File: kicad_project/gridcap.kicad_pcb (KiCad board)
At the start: 2 copper layers, 119.1 x 108.7 mm, 69 parts, among them J1 Conn_01x10

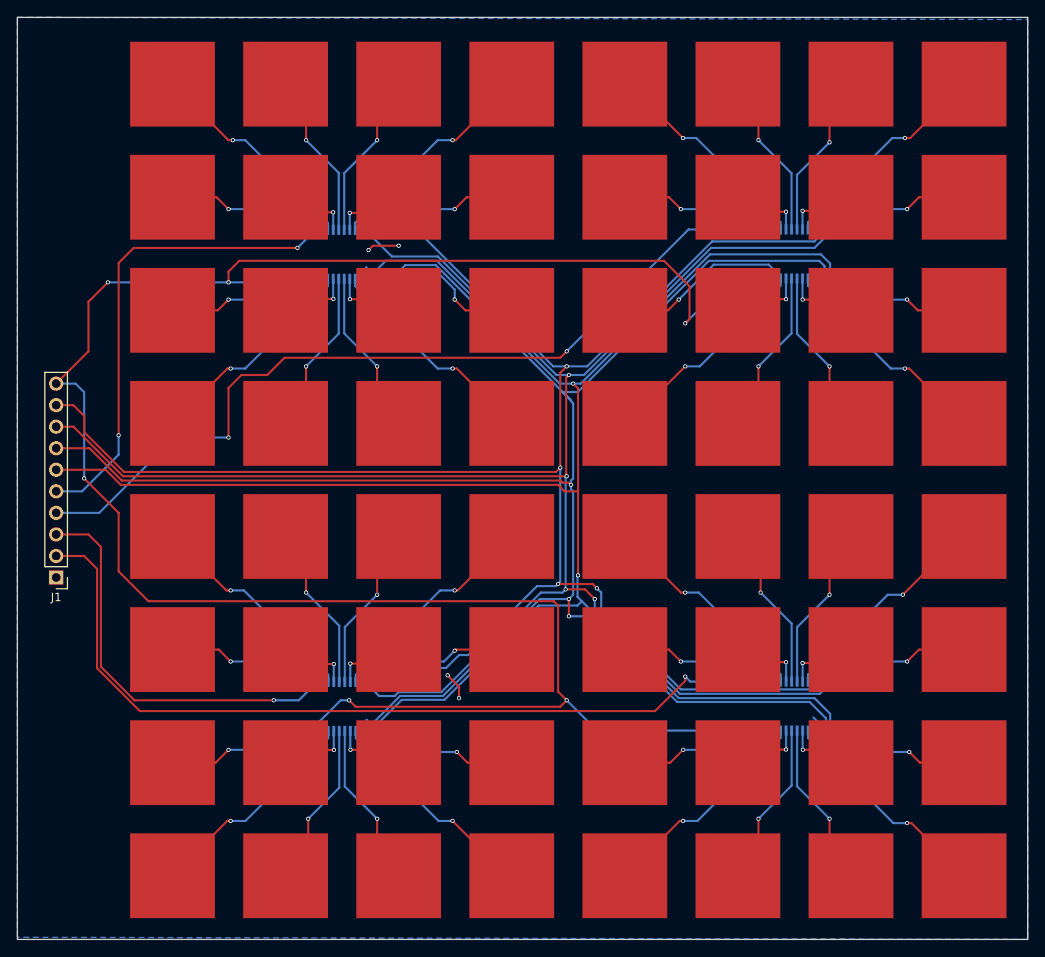
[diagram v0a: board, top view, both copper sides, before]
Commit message: Space out tracks on pcb
Meant to reduce signal noice between tracks
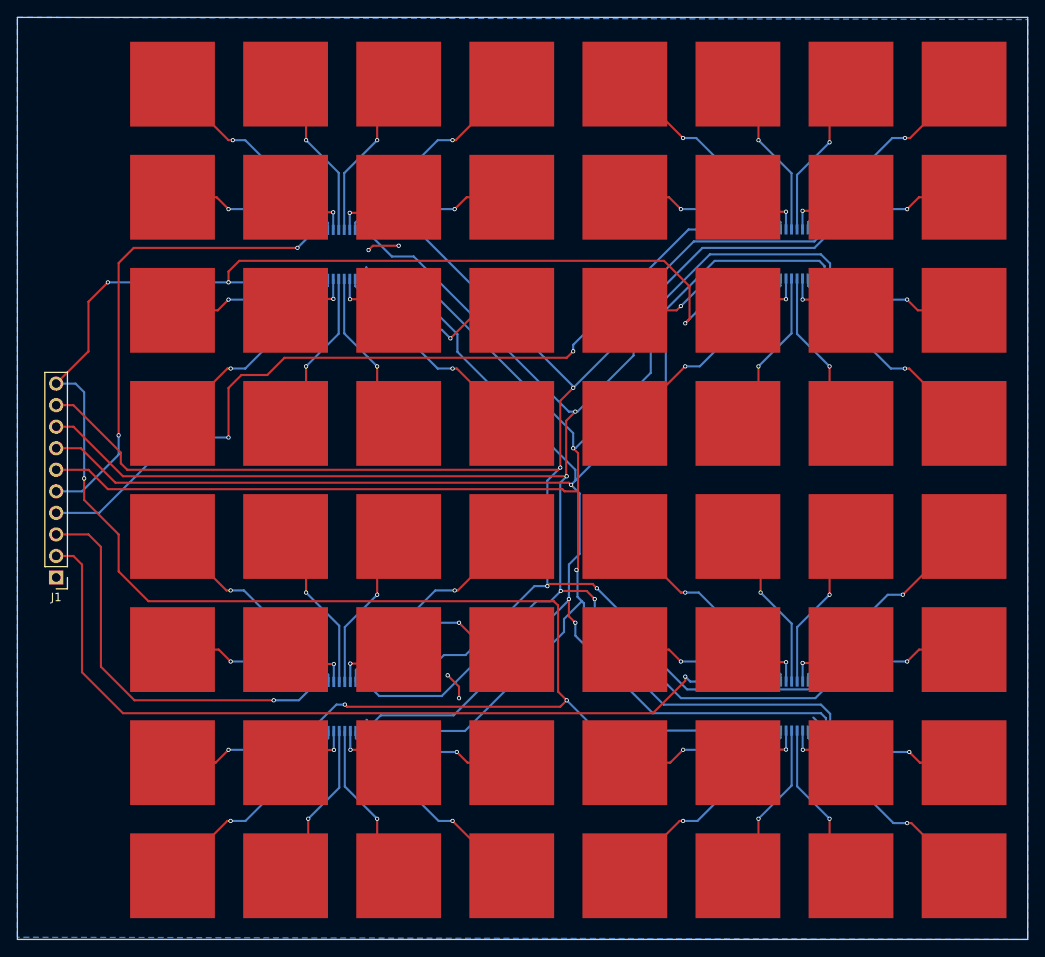
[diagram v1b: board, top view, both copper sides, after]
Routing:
- net S3: track 225.8 -> 229.2 mm
- net S1: track 223.3 -> 226.5 mm
- net S2: track 228.0 -> 231.2 mm
- net Net-(MUX3-Y0): track 19.8 -> 22.4 mm
- net S0: track 224.8 -> 226.3 mm
- net Z4: track 100.8 -> 101.6 mm

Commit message: Make MUX-pads longer
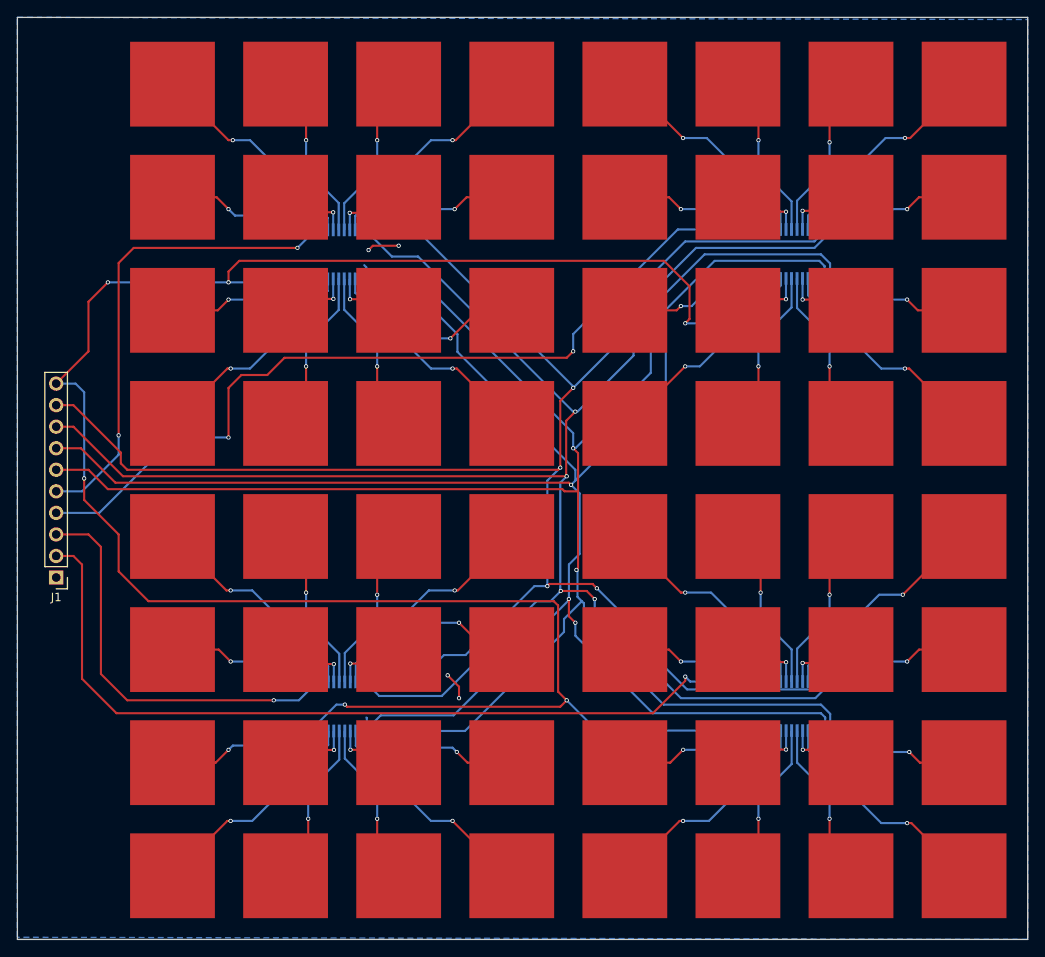
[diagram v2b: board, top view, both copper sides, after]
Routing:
- net GND: track 15.2 -> 17.9 mm
- net Net-(MUX4-Y6): track 25.9 -> 26.8 mm
- net Net-(MUX4-Y14): track 26.0 -> 26.8 mm
- net Net-(MUX4-Y9): track 26.0 -> 26.7 mm
- net Z2: track 101.8 -> 102.6 mm
- net Net-(MUX2-Y6): track 25.9 -> 26.7 mm
- net Net-(MUX2-Y14): track 26.0 -> 26.6 mm
- net Net-(MUX4-Y1): track 26.0 -> 26.6 mm
- net S0: track 226.3 -> 226.9 mm
- net Net-(MUX3-Y6): track 26.0 -> 26.5 mm
- net Net-(MUX3-Y14): track 26.0 -> 26.5 mm
